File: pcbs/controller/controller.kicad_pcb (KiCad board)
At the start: 2 copper layers, 38 x 29 mm, 8 parts, among them J1 Conn_01x11, J2 Conn_01x02, J3 Conn_01x02, U1 XIAO-nRF52840-SMD

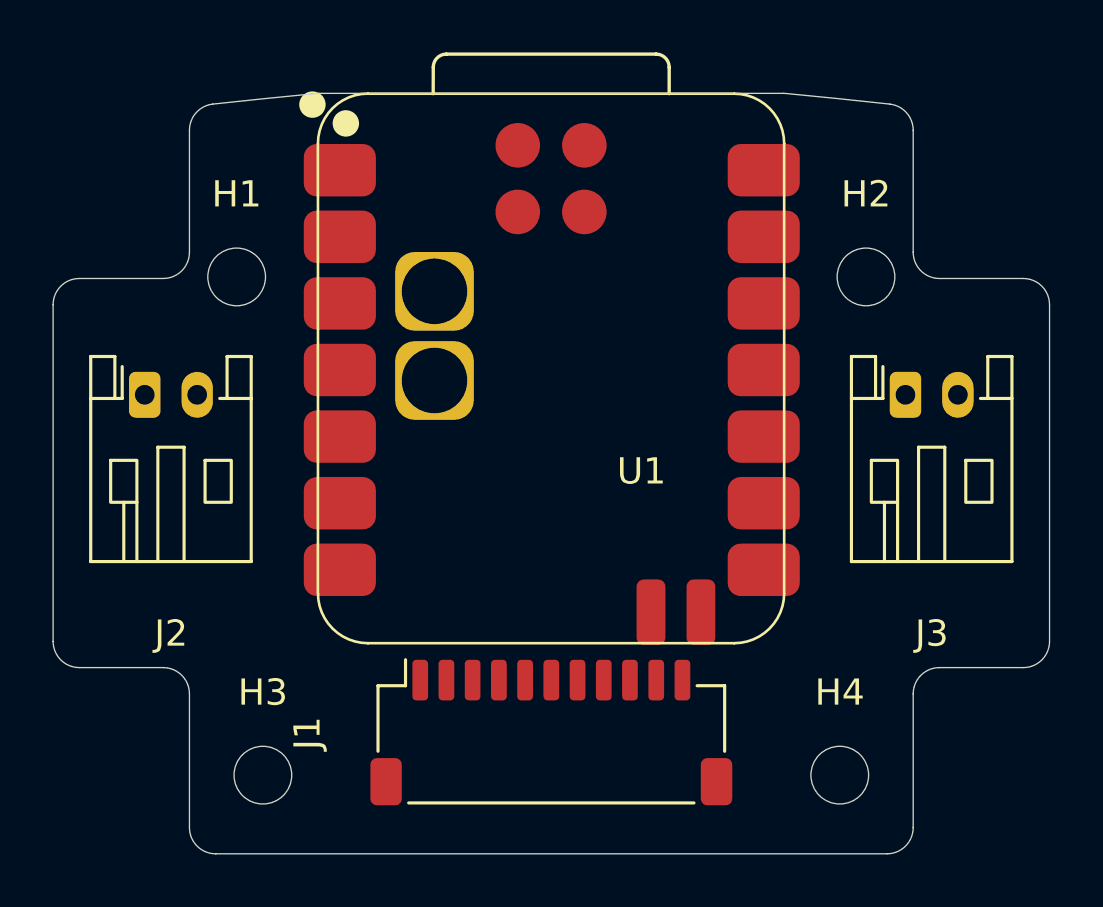
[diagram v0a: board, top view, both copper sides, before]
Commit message: Route the controller board
Power on B.Cu (0.5 mm): J2 / J3 to the XIAO battery pads (U1-19 VBAT,
U1-20 GND), clear of B.Cu keepout rule areas (r 3) for the lid
pedestals under H1-H4.

Signals on F.Cu (0.25 mm), all single layer. The H1 screw head blocks
the outside of the top three left pins, and the B.Cu power traces cross
under the XIAO, so D0-D2 run under the module and enter J1 from behind.
D3-D6 and D7-D10 run outside the XIAO and enter J1 from the front,
under the connector body. J1 is reassigned to suit: pins 1-11 =
D6 D5 D4 D3 D2 D1 D0 D10 D9 D8 D7, so with a straight cable
D0-D6 = C0-C6 and D7-D10 = R0-R3.

Also reapply the controller Edge.Cuts after the 6.25-degree tilt
change.

Co-Authored-By: Claude Opus 5.5 <noreply@anthropic.com>
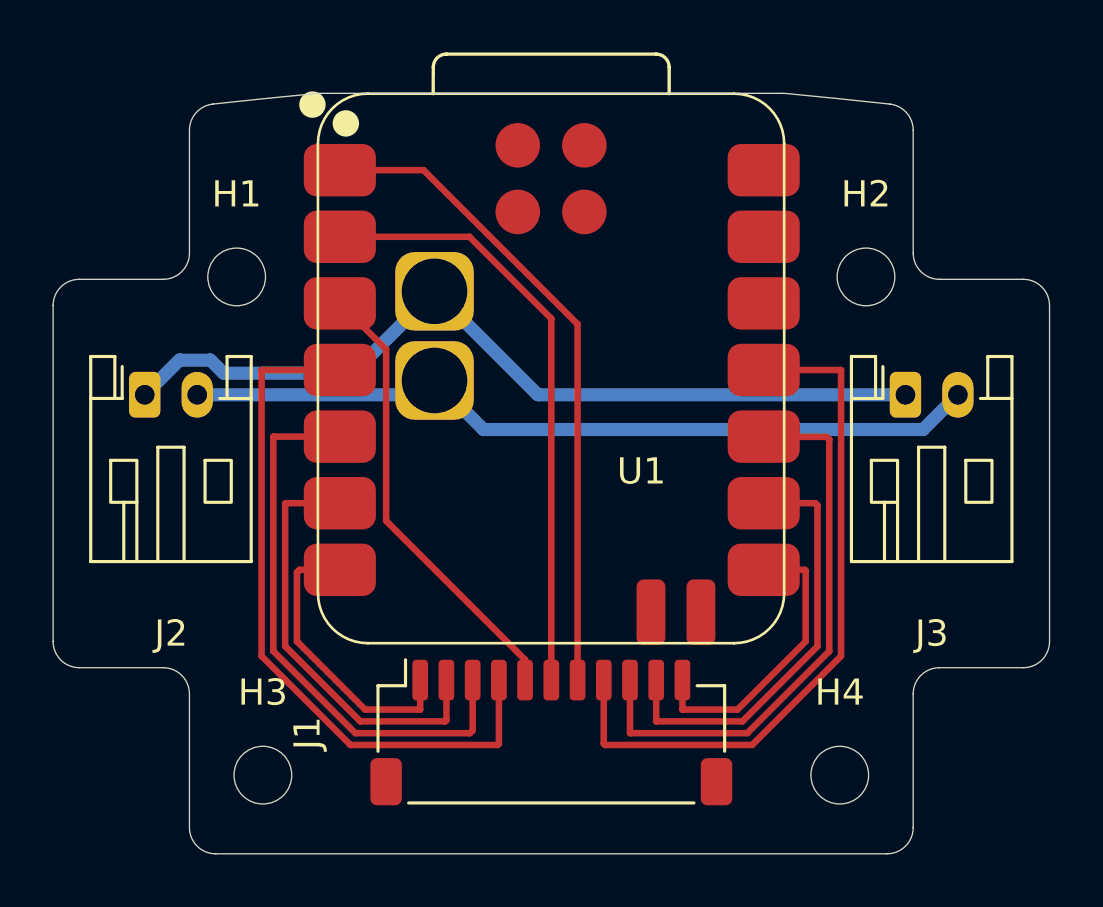
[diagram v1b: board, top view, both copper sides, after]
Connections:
- J1 pad 1: /D0 -> /D6
- J1 pad 10: /D9 -> /D8
- J1 pad 11: /D10 -> /D7
- J1 pad 2: /D1 -> /D5
- J1 pad 3: /D2 -> /D4
- J1 pad 5: /D4 -> /D2
- J1 pad 6: /D5 -> /D1
- J1 pad 7: /D6 -> /D0
- J1 pad 8: /D7 -> /D10
- J1 pad 9: /D8 -> /D9
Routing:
- net /GND: track 0.00 -> 32.7 mm
- net /VBAT: track 0.00 -> 30.6 mm
- net /D3: track 0.00 -> 26.8 mm
- net /D10: track 0.00 -> 26.8 mm
- net /D0: track 0.00 -> 25.1 mm
- net /D1: track 0.00 -> 23.1 mm
- net /D4: track 0.00 -> 21.6 mm
- net /D9: track 0.00 -> 21.5 mm
- net /D2: track 0.00 -> 17.3 mm
- net /D5: track 0.00 -> 16.4 mm
- net /D8: track 0.00 -> 16.4 mm
- net /D7: track 0.00 -> 11.2 mm
- net /D6: track 0.00 -> 11.2 mm

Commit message: Clean up short track segments on the controller board
Remove track stubs left inside pads (D2, D9, GND, VBAT) and merge the
tiny corner segments on D4, D5 and D7 so every corner is a single
point. DRC is unchanged: no unconnected items or clearance errors.

Co-Authored-By: Claude Opus 5.5 <noreply@anthropic.com>
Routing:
- net /VBAT: track 30.6 -> 29.8 mm
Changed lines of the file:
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@@
+	)
+	(segment
+		(start 93.7 102.3)
+		(end 99 107.6)
+		(width 0.25)
+		(layer "F.Cu")
+		(net "/D2")
+	)
+	(segment
+		(start 93.7 99.766002)
+		(end 93.7 102.3)
+		(width 0.25)
+		(layer "F.Cu")
+		(net "/D2")
+	)
+	(segment
+		(start 99 107.6)
+		(end 99 112.375)
+		(width 0.25)
+		(layer "F.Cu")
+		(net "/D2")
 	)
 	(segment
@@
 	)
 	(segment
-		(start 99 111.600001)
-		(end 99 112.375)
-		(width 0.25)
-		(layer "F.Cu")
-		(net "/D2")
-	)
-	(segment
-		(start 93.7 99.766002)
-		(end 93.7 106.300001)
-		(width 0.25)
-		(layer "F.Cu")
-		(net "/D2")
-	)
-	(segment
-		(start 93.7 106.300001)
-		(end 99 111.600001)
-		(width 0.25)
-		(layer "F.Cu")
-		(net "/D2")
-	)
-	(segment
-		(start 91.935 98.01)
-		(end 91.943998 98.01)
-		(width 0.25)
-		(layer "F.Cu")
-		(net "/D2")
-	)
-	(segment
 		(start 88.95 111.459188)
 		(end 92.340812 114.85)
@@
 	)
 	(segment
-		(start 89.41 103.09)
-		(end 89.4 103.1)
-		(width 0.25)
-		(layer "F.Cu")
-		(net "/D4")
-	)
-	(segment
 		(start 97 114.3)
 		(end 97 112.375)
@@
 	)
 	(segment
-		(start 89.4 103.1)
+		(start 89.4 111.272792)
+		(end 92.527208 114.4)
+		(width 0.25)
+		(layer "F.Cu")
+		(net "/D4")
+	)
+	(segment
+		(start 91.935 103.09)
+		(end 89.4 103.09)
+		(width 0.25)
+		(layer "F.Cu")
+		(net "/D4")
+	)
+	(segment
+		(start 89.4 103.09)
 		(end 89.4 111.272792)
 		(width 0.25)
@@
 	)
 	(segment
-		(start 91.935 103.09)
-		(end 89.41 103.09)
-		(width 0.25)
-		(layer "F.Cu")
-		(net "/D4")
-	)
-	(segment
-		(start 89.4 111.272792)
-		(end 92.527208 114.4)
-		(width 0.25)
-		(layer "F.Cu")
-		(net "/D4")
+		(start 89.85 105.63)
+		(end 89.85 111.086396)
+		(width 0.25)
+		(layer "F.Cu")
+		(net "/D5")
 	)
 	(segment
@@
 	)
 	(segment
-		(start 89.85 105.65)
-		(end 89.85 111.086396)
-		(width 0.25)
-		(layer "F.Cu")
-		(net "/D5")
-	)
-	(segment
 		(start 89.85 111.086396)
 		(end 92.713604 113.95)
@@
 	)
 	(segment
-		(start 91.935 105.63)
-		(end 89.87 105.63)
-		(width 0.25)
-		(layer "F.Cu")
-		(net "/D5")
-	)
-	(segment
 		(start 92.713604 113.95)
 		(end 95.95 113.95)
@@
 	)
 	(segment
-		(start 89.87 105.63)
-		(end 89.85 105.65)
-		(width 0.25)
-		(layer "F.Cu")
-		(net "/D5")
-	)
-	(segment
-		(start 90.4 108.17)
-		(end 90.3 108.27)
+		(start 91.935 105.63)
+		(end 89.85 105.63)
+		(width 0.25)
+		(layer "F.Cu")
+		(net "/D5")
+	)
+	(segment
+		(start 91.935 108.17)
+		(end 90.3 108.17)
+		(width 0.25)
+		(layer "F.Cu")
+		(net "/D6")
+	)
+	(segment
+		(start 95 113.5)
+		(end 95 112.375)
 		(width 0.25)
 		(layer "F.Cu")
@@
 	)
 	(segment
-		(start 91.935 108.17)
-		(end 90.4 108.17)
+		(start 90.3 108.17)
+		(end 90.3 110.9)
 		(width 0.25)
 		(layer "F.Cu")
@@
 	)
 	(segment
-		(start 95 113.5)
-		(end 95 112.375)
-		(width 0.25)
-		(layer "F.Cu")
-		(net "/D6")
-	)
-	(segment
-		(start 90.3 108.27)
-		(end 90.3 110.9)
-		(width 0.25)
-		(layer "F.Cu")
-		(net "/D6")
-	)
-	(segment
-		(start 109.67 108.17)
-		(end 109.7 108.2)
-		(width 0.25)
-		(layer "F.Cu")
-		(net "/D7")
-	)
-	(segment
-		(start 108.1 108.17)
-		(end 109.67 108.17)
-		(width 0.25)
-		(layer "F.Cu")
-		(net "/D7")
-	)
-	(segment
-		(start 109.7 108.2)
-		(end 109.7 110.9)
+		(start 105 113.5)
+		(end 105 112.375)
 		(width 0.25)
 		(layer "F.Cu")
@@
 	)
 	(segment
-		(start 105 113.5)
-		(end 105 112.375)
+		(start 109.7 108.17)
+		(end 109.7 110.9)
+		(width 0.25)
+		(layer "F.Cu")
+		(net "/D7")
+	)
+	(segment
+		(start 108.1 108.17)
+		(end 109.7 108.17)
 		(width 0.25)
 		(layer "F.Cu")
@@
 	)
 	(segment
-		(start 110.07 105.63)
-		(end 110.15 105.71)
+		(start 104 112.375)
+		(end 104 113.95)
 		(width 0.25)
 		(layer "F.Cu")
@@
 	(segment
 		(start 107.286396 113.95)
-		(end 104 113.95)
+		(end 110.15 111.086396)
 		(width 0.25)
 		(layer "F.Cu")
@@
 	)
 	(segment
-		(start 110.15 105.71)
-		(end 110.15 111.086396)
+		(start 110.15 105.63)
+		(end 108.1 105.63)
 		(width 0.25)
 		(layer "F.Cu")
@@
 	)
 	(segment
-		(start 108.1 105.63)
-		(end 110.07 105.63)
+		(start 110.15 111.086396)
+		(end 110.15 105.63)
 		(width 0.25)
 		(layer "F.Cu")
@@
 	)
 	(segment
-		(start 110.15 111.086396)
+		(start 104 113.95)
 		(end 107.286396 113.95)
 		(width 0.25)
@@
 	)
 	(segment
-		(start 104 113.95)
-		(end 104 112.375)
-		(width 0.25)
-		(layer "F.Cu")
-		(net "/D8")
-	)
-	(segment
 		(start 108.1 103.09)
-		(end 108.11 103.1)
-		(width 0.25)
-		(layer "F.Cu")
-		(net "/D9")
-	)
-	(segment
-		(start 108.11 103.1)
-		(end 110.5 103.1)
+		(end 110.6 103.09)
 		(width 0.25)
 		(layer "F.Cu")
@@
 	)
 	(segment
-		(start 110.6 103.2)
+		(start 110.6 103.09)
 		(end 110.6 111.272792)
 		(width 0.25)
@@
 	)
 	(segment
-		(start 110.5 103.1)
-		(end 110.6 103.2)
+		(start 107.472792 114.4)
+		(end 103 114.4)
 		(width 0.25)
 		(layer "F.Cu")
@@
 	)
 	(segment
-		(start 107.472792 114.4)
-		(end 103 114.4)
-		(width 0.25)
-		(layer "F.Cu")
-		(net "/D9")
-	)
-	(segment
 		(start 111.05 100.55)
 		(end 111.05 111.459188)
@@
 	)
 	(segment
-		(start 95.545 100.95)
-		(end 95 101.495)
-		(width 0.5)
-		(layer "B.Cu")
-		(net "/VBAT")
-	)
-	(segment
 		(start 95 101.495)
 		(end 86.495 101.495)
@@
 		(width 0.5)
 		(layer "B.Cu")
-		(net "/GND")
-	)
-	(segment
-		(start 95.545 97.55)
-		(end 95.55 97.55)
-		(width 0.5)
-		(layer "B.Cu")

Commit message: Label the battery connectors and the board on the back silkscreen
Add B.Silkscreen text: the polarity of J2 / J3 (- = pin 1 GND,
+ = pin 2 VBAT) with "BAT L" / "BAT R" for the hand each is used on,
and "optokbd controller / v0.2.0 2026-10" between the H3 and H4
pedestals. scripts/add_silk_labels.py places them from the KiCad
scripting console and replaces its own text when run again.

Co-Authored-By: Claude Opus 5.5 <noreply@anthropic.com>
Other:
- board text added: "+"
- board text added: "-"
- board text added: "BAT L"
- board text added: "BAT R"
- board text added: "optokbd controller v0.2.0 2026-10"
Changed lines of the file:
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@@
 		(layer "Edge.Cuts")
+	)
+	(gr_text "optokbd controller\nv0.2.0 2026-10"
+		(at 100 116.5 0)
+		(layer "B.SilkS")
+		(effects
+			(font
+				(size 0.8 0.8)
+				(thickness 0.15)
+			)
+			(justify mirror)
+		)
+	)
+	(gr_text "-"
+		(at 84.495 103.3 0)
+		(layer "B.SilkS")
+		(effects
+			(font
+				(size 1 1)
+				(thickness 0.15)
+			)
+			(justify mirror)
+		)
+	)
+	(gr_text "BAT L"
+		(at 85.495 104.8 0)
+		(layer "B.SilkS")
+		(effects
+			(font
+				(size 1 1)
+				(thickness 0.15)
+			)
+			(justify mirror)
+		)
+	)
+	(gr_text "+"
+		(at 86.495 103.3 0)
+		(layer "B.SilkS")
+		(effects
+			(font
+				(size 1 1)
+				(thickness 0.15)
+			)
+			(justify mirror)
+		)
+	)
+	(gr_text "-"
+		(at 113.505 103.3 0)
+		(layer "B.SilkS")
+		(effects
+			(font
+				(size 1 1)
+				(thickness 0.15)
+			)
+			(justify mirror)
+		)
+	)
+	(gr_text "BAT R"
+		(at 114.505 104.8 0)
+		(layer "B.SilkS")
+		(effects
+			(font
+				(size 1 1)
+				(thickness 0.15)
+			)
+			(justify mirror)
+		)
+	)
+	(gr_text "+"
+		(at 115.505 103.3 0)
+		(layer "B.SilkS")
+		(effects
+			(font
+				(size 1 1)
+				(thickness 0.15)
+			)
+			(justify mirror)
+		)
 	)
 	(segment

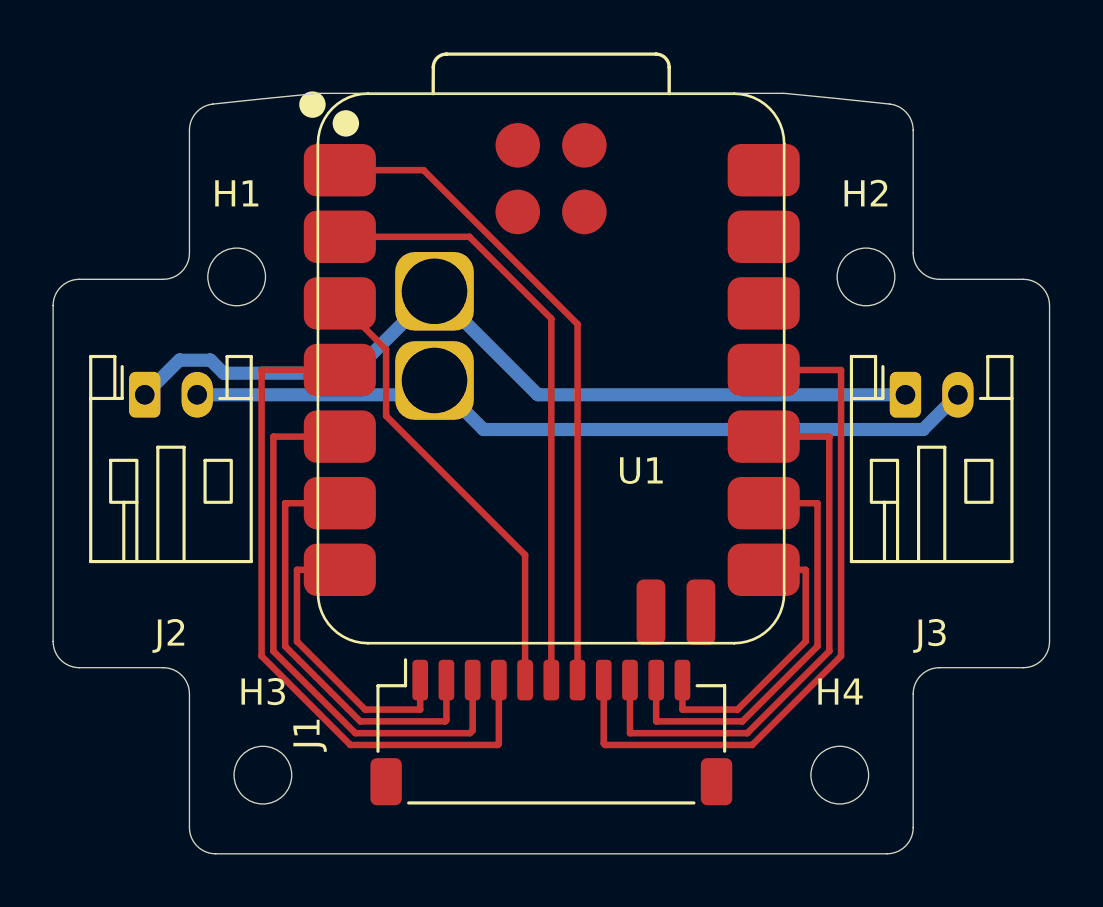
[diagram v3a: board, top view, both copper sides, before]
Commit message: Round the controller board traces and add teardrops
Fillet the trace corners with arcs (widths unchanged) and add
teardrops. Drop the teardrops on U1-3 (D2) and U1-20 (GND) and turn
them off for those pads: they reached within 0.001 mm of U1-4 (D3)
and 0.09 mm of U1-19 (VBAT), which DRC did not flag. The remaining
teardrops keep at least 0.2 mm from other nets. DRC: no unconnected
items or errors.

Co-Authored-By: Claude Opus 5.5 <noreply@anthropic.com>
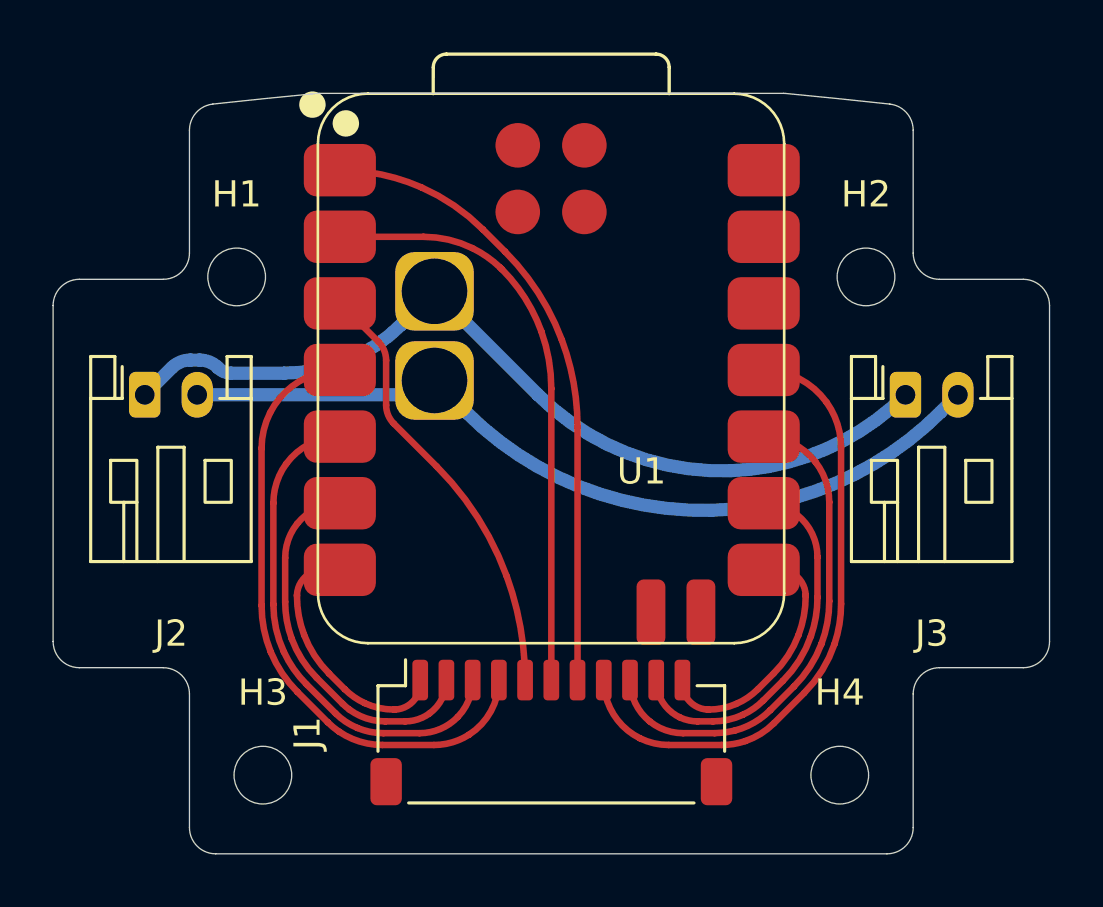
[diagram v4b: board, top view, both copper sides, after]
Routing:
- net /D3: track 26.8 -> 24.1 mm
- net /D10: track 26.8 -> 24.1 mm
- net /D9: track 21.6 -> 19.3 mm
- net /D4: track 21.6 -> 19.3 mm
- net /D8: track 16.4 -> 14.4 mm
- net /D5: track 16.4 -> 14.6 mm
- net /VBAT: track 29.8 -> 31.1 mm
- net /D6: track 11.3 -> 10.0 mm
- net /D7: track 11.2 -> 10.00 mm
- net /GND: track 32.7 -> 33.7 mm
- net /D0: track 25.1 -> 24.3 mm
- net /D2: track 17.3 -> 16.7 mm
